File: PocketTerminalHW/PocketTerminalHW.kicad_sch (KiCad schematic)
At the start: 182 parts, among them J1 USB4105-GF-A, J2 DM3D-SF, J3 Conn_01x05, J4 53261-0271, J5 Conn_01x04, J6 Conn_01x02, J7 68712414522, J8 USB4105-GF-A, J9 66011102111302, Q1 BC847BDW1, SW1 K3-1391D-5MM, U1 ESP32-S3-WROOM-1, U2 CP2102N-A02-GQFN28, U3 AMS1117-3.3 / SGM2212-3.3, U4 TP4057, U5 MT3608/SX1308, U6 CC1101RGPR, Y1 3225-26M-SR

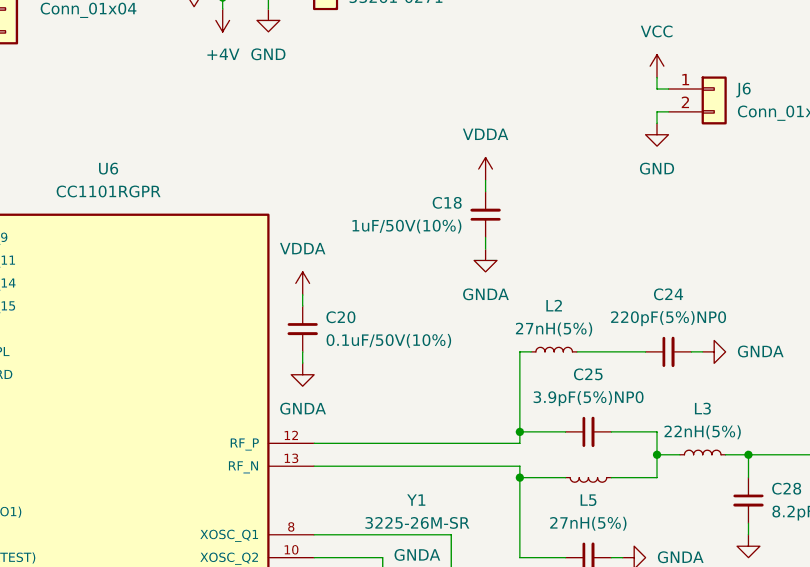
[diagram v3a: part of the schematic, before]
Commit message: Minor cnages to cap values
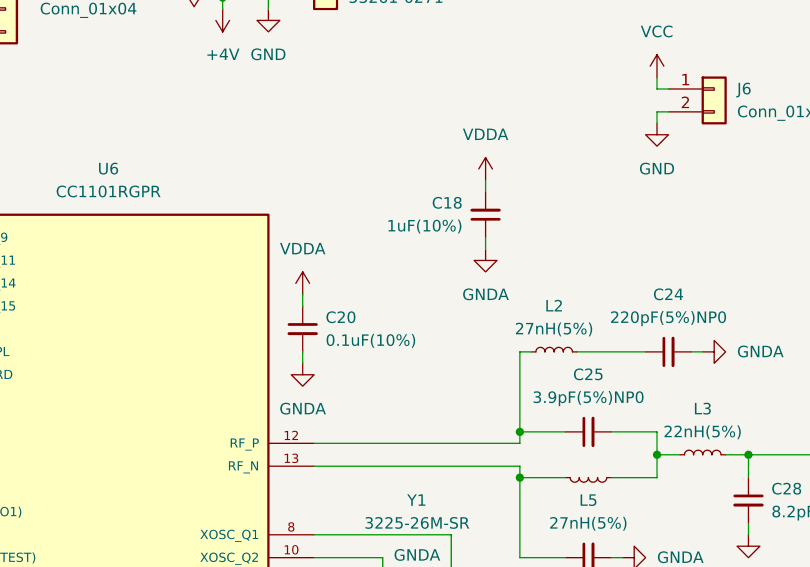
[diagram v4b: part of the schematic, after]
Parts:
- C18: value 1uF/50V(10%) -> 1uF(10%)
- C20: value 0.1uF/50V(10%) -> 0.1uF(10%)
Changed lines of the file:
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@@
 		(row_heights 2.54 2.54 2.54 2.54 2.54)
 		(cells
-			(table_cell "EN"
+			(table_cell "IO0"
 				(exclude_from_sim no)
-				(at 170.18 127 0)
+				(at 175.26 127 0)
 				(size 5.08 2.54)
 				(margins 0.9525 0.9525 0.9525 0.9525)
@@
 			(table_cell "1"
 				(exclude_from_sim no)
-				(at 170.18 129.54 0)
+				(at 175.26 129.54 0)
 				(size 5.08 2.54)
 				(margins 0.9525 0.9525 0.9525 0.9525)
@@
 			(table_cell "1"
 				(exclude_from_sim no)
-				(at 170.18 132.08 0)
+				(at 175.26 132.08 0)
 				(size 5.08 2.54)
 				(margins 0.9525 0.9525 0.9525 0.9525)
@@
 				)
 			)
-			(table_cell "0"
+			(table_cell "1"
 				(exclude_from_sim no)
-				(at 170.18 134.62 0)
+				(at 175.26 134.62 0)
 				(size 5.08 2.54)
 				(margins 0.9525 0.9525 0.9525 0.9525)
@@
 				)
 			)
-			(table_cell "1"
+			(table_cell "0"
 				(exclude_from_sim no)
-				(at 170.18 137.16 0)
+				(at 175.26 137.16 0)
 				(size 5.08 2.54)
 				(margins 0.9525 0.9525 0.9525 0.9525)
@@
 		(row_heights 2.54 2.54 2.54 2.54 2.54)
 		(cells
-			(table_cell "IO0"
+			(table_cell "DTR"
 				(exclude_from_sim no)
-				(at 175.26 127 0)
+				(at 160.02 127 0)
 				(size 5.08 2.54)
 				(margins 0.9525 0.9525 0.9525 0.9525)
@@
 			(table_cell "1"
 				(exclude_from_sim no)
-				(at 175.26 129.54 0)
+				(at 160.02 129.54 0)
 				(size 5.08 2.54)
 				(margins 0.9525 0.9525 0.9525 0.9525)
@@
 				)
 			)
-			(table_cell "1"
+			(table_cell "0"
 				(exclude_from_sim no)
-				(at 175.26 132.08 0)
+				(at 160.02 132.08 0)
 				(size 5.08 2.54)
 				(margins 0.9525 0.9525 0.9525 0.9525)
@@
 			(table_cell "1"
 				(exclude_from_sim no)
-				(at 175.26 134.62 0)
+				(at 160.02 134.62 0)
 				(size 5.08 2.54)
 				(margins 0.9525 0.9525 0.9525 0.9525)
@@
 			(table_cell "0"
 				(exclude_from_sim no)
-				(at 175.26 137.16 0)
+				(at 160.02 137.16 0)
 				(size 5.08 2.54)
 				(margins 0.9525 0.9525 0.9525 0.9525)
@@
 		(row_heights 2.54 2.54 2.54 2.54 2.54)
 		(cells
-			(table_cell "DTR"
+			(table_cell "EN"
 				(exclude_from_sim no)
-				(at 160.02 127 0)
+				(at 170.18 127 0)
 				(size 5.08 2.54)
 				(margins 0.9525 0.9525 0.9525 0.9525)
@@
 			(table_cell "1"
 				(exclude_from_sim no)
-				(at 160.02 129.54 0)
+				(at 170.18 129.54 0)
 				(size 5.08 2.54)
 				(margins 0.9525 0.9525 0.9525 0.9525)
@@
 				)
 			)
-			(table_cell "0"
+			(table_cell "1"
 				(exclude_from_sim no)
-				(at 160.02 132.08 0)
+				(at 170.18 132.08 0)
 				(size 5.08 2.54)
 				(margins 0.9525 0.9525 0.9525 0.9525)
@@
 				)
 			)
-			(table_cell "1"
+			(table_cell "0"
 				(exclude_from_sim no)
-				(at 160.02 134.62 0)
+				(at 170.18 134.62 0)
 				(size 5.08 2.54)
 				(margins 0.9525 0.9525 0.9525 0.9525)
@@
 				)
 			)
-			(table_cell "0"
+			(table_cell "1"
 				(exclude_from_sim no)
-				(at 160.02 137.16 0)
+				(at 170.18 137.16 0)
 				(size 5.08 2.54)
 				(margins 0.9525 0.9525 0.9525 0.9525)
@@
 			)
 		)
-		(property "Value" "1uF/50V(10%)"
+		(property "Value" "1uF(10%)"
 			(at 273.05 199.3835 0)
 			(effects
@@
 			)
 		)
-		(property "Value" "0.1uF/50V(10%)"
+		(property "Value" "0.1uF(10%)"
 			(at 257.81 212.0962 0)
 			(effects

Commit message: Second proto WIP
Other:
- note added: "TODO: Add some power circuit to not use battery while charging"
- note added: "TODO: Maybe move components to the front side, under display"
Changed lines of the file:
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@@
 		)
 	)
+	(text "TODO: Maybe move components to the front side, under display"
+		(exclude_from_sim no)
+		(at 311.912 171.958 0)
+		(effects
+			(font
+				(size 1.27 1.27)
+			)
+		)
+	)
+	(text "TODO: Add some power circuit to not use battery while charging"
+		(exclude_from_sim no)
+		(at 312.42 174.244 0)
+		(effects
+			(font
+				(size 1.27 1.27)
+			)
+		)
+	)
 	(text "TODO: Add USB protection"
 		(exclude_from_sim no)
@@
 		(row_heights 2.54 2.54 2.54 2.54 2.54)
 		(cells
-			(table_cell "IO0"
+			(table_cell "RTS"
 				(exclude_from_sim no)
-				(at 175.26 127 0)
+				(at 165.1 127 0)
 				(size 5.08 2.54)
 				(margins 0.9525 0.9525 0.9525 0.9525)
@@
 			(table_cell "1"
 				(exclude_from_sim no)
-				(at 175.26 129.54 0)
+				(at 165.1 129.54 0)
 				(size 5.08 2.54)
 				(margins 0.9525 0.9525 0.9525 0.9525)
@@
 				)
 			)
-			(table_cell "1"
+			(table_cell "0"
 				(exclude_from_sim no)
-				(at 175.26 132.08 0)
+				(at 165.1 132.08 0)
 				(size 5.08 2.54)
 				(margins 0.9525 0.9525 0.9525 0.9525)
@@
 				)
 			)
-			(table_cell "1"
+			(table_cell "0"
 				(exclude_from_sim no)
-				(at 175.26 134.62 0)
+				(at 165.1 134.62 0)
 				(size 5.08 2.54)
 				(margins 0.9525 0.9525 0.9525 0.9525)
@@
 				)
 			)
-			(table_cell "0"
+			(table_cell "1"
 				(exclude_from_sim no)
-				(at 175.26 137.16 0)
+				(at 165.1 137.16 0)
 				(size 5.08 2.54)
 				(margins 0.9525 0.9525 0.9525 0.9525)
@@
 	)
 	(table
-		(column_count 1)
+		(column_count 2)
 		(border
 			(external yes)
@@
 			)
 		)
-		(column_widths 5.08)
-		(row_heights 2.54 2.54 2.54 2.54 2.54)
+		(column_widths 5.715 6.985)
+		(row_heights 2.54 2.54 2.54 2.54 2.54 2.54)
 		(cells
-			(table_cell "DTR"
+			(table_cell "R"
 				(exclude_from_sim no)
-				(at 160.02 127 0)
-				(size 5.08 2.54)
+				(at 317.5 152.4 0)
+				(size 5.715 2.54)
 				(margins 0.9525 0.9525 0.9525 0.9525)
 				(span 1 1)
@@
 						(size 1.27 1.27)
 					)
-					(justify left top)
+					(justify top)
 				)
 			)
-			(table_cell "1"
+			(table_cell "I"
 				(exclude_from_sim no)
-				(at 160.02 129.54 0)
-				(size 5.08 2.54)
+				(at 323.215 152.4 0)
+				(size 6.985 2.54)
 				(margins 0.9525 0.9525 0.9525 0.9525)
 				(span 1 1)
@@
 						(size 1.27 1.27)
 					)
-					(justify left top)
+					(justify top)
 				)
 			)
-			(table_cell "0"
+			(table_cell "5K"
 				(exclude_from_sim no)
-				(at 160.02 132.08 0)
-				(size 5.08 2.54)
+				(at 317.5 154.94 0)
+				(size 5.715 2.54)
 				(margins 0.9525 0.9525 0.9525 0.9525)
 				(span 1 1)
@@
 				)
 			)
-			(table_cell "1"
+			(table_cell "0.2A"
 				(exclude_from_sim no)
-				(at 160.02 134.62 0)
-				(size 5.08 2.54)
+				(at 323.215 154.94 0)
+				(size 6.985 2.54)
 				(margins 0.9525 0.9525 0.9525 0.9525)
 				(span 1 1)
@@
 				)
 			)
-			(table_cell "0"
+			(table_cell "4K"
 				(exclude_from_sim no)
-				(at 160.02 137.16 0)
-				(size 5.08 2.54)
+				(at 317.5 157.48 0)
+				(size 5.715 2.54)
 				(margins 0.9525 0.9525 0.9525 0.9525)
 				(span 1 1)
@@
 				)
 			)
-		)
-	)
-	(table
-		(column_count 2)
-		(border
-			(external yes)
-			(header yes)
-			(stroke
-				(width 0)
-				(type solid)
-			)
-		)
-		(separators
-			(rows yes)
-			(cols yes)
-			(stroke
-				(width 0)
-				(type solid)
-			)
-		)
-		(column_widths 5.715 6.985)
-		(row_heights 2.54 2.54 2.54 2.54 2.54 2.54)
-		(cells
-			(table_cell "R"
+			(table_cell "0.25A"
 				(exclude_from_sim no)
-				(at 317.5 152.4 0)
-				(size 5.715 2.54)
+				(at 323.215 157.48 0)
+				(size 6.985 2.54)
 				(margins 0.9525 0.9525 0.9525 0.9525)
 				(span 1 1)
@@
 						(size 1.27 1.27)
 					)
-					(justify top)
+					(justify left top)
 				)
 			)
-			(table_cell "I"
+			(table_cell "3K"
 				(exclude_from_sim no)
-				(at 323.215 152.4 0)
-				(size 6.985 2.54)
+				(at 317.5 160.02 0)
+				(size 5.715 2.54)
 				(margins 0.9525 0.9525 0.9525 0.9525)
 				(span 1 1)
@@
 						(size 1.27 1.27)
 					)
-					(justify top)
+					(justify left top)
 				)
 			)
-			(table_cell "5K"
+			(table_cell "0.3A"
 				(exclude_from_sim no)
-				(at 317.5 154.94 0)
-				(size 5.715 2.54)
+				(at 323.215 160.02 0)
+				(size 6.985 2.54)
 				(margins 0.9525 0.9525 0.9525 0.9525)
 				(span 1 1)
@@
 				)
 			)
-			(table_cell "0.2A"
+			(table_cell "2K"
 				(exclude_from_sim no)
-				(at 323.215 154.94 0)
-				(size 6.985 2.54)
+				(at 317.5 162.56 0)
+				(size 5.715 2.54)
 				(margins 0.9525 0.9525 0.9525 0.9525)
 				(span 1 1)
@@
 				)
 			)
-			(table_cell "4K"
+			(table_cell "0.4A"
 				(exclude_from_sim no)
-				(at 317.5 157.48 0)
-				(size 5.715 2.54)
+				(at 323.215 162.56 0)
+				(size 6.985 2.54)
 				(margins 0.9525 0.9525 0.9525 0.9525)
 				(span 1 1)
@@
 				)
 			)
-			(table_cell "0.25A"
+			(table_cell "1.6K"
 				(exclude_from_sim no)
-				(at 323.215 157.48 0)
-				(size 6.985 2.54)
+				(at 317.5 165.1 0)
+				(size 5.715 2.54)
 				(margins 0.9525 0.9525 0.9525 0.9525)
 				(span 1 1)
@@
 				)
 			)
-			(table_cell "3K"
+			(table_cell "0.5A"
 				(exclude_from_sim no)
-				(at 317.5 160.02 0)
-				(size 5.715 2.54)
+				(at 323.215 165.1 0)
+				(size 6.985 2.54)
 				(margins 0.9525 0.9525 0.9525 0.9525)
 				(span 1 1)
@@
 				)
 			)
-			(table_cell "0.3A"
+		)
+	)
+	(table
+		(column_count 1)
+		(border
+			(external yes)
+			(header yes)
+			(stroke
+				(width 0)
+				(type solid)
+			)
+		)
+		(separators
+			(rows yes)
+			(cols yes)
+			(stroke
+				(width 0)
+				(type solid)
+			)
+		)
+		(column_widths 5.08)
+		(row_heights 2.54 2.54 2.54 2.54 2.54)
+		(cells
+			(table_cell "IO0"
 				(exclude_from_sim no)
-				(at 323.215 160.02 0)
-				(size 6.985 2.54)
+				(at 175.26 127 0)
+				(size 5.08 2.54)
 				(margins 0.9525 0.9525 0.9525 0.9525)
 				(span 1 1)
@@
 				)
 			)
-			(table_cell "2K"
+			(table_cell "1"
 				(exclude_from_sim no)
-				(at 317.5 162.56 0)
-				(size 5.715 2.54)
+				(at 175.26 129.54 0)
+				(size 5.08 2.54)
 				(margins 0.9525 0.9525 0.9525 0.9525)
 				(span 1 1)
@@
 				)
 			)
-			(table_cell "0.4A"
+			(table_cell "1"
 				(exclude_from_sim no)
-				(at 323.215 162.56 0)
-				(size 6.985 2.54)
+				(at 175.26 132.08 0)
+				(size 5.08 2.54)
 				(margins 0.9525 0.9525 0.9525 0.9525)
 				(span 1 1)
@@
 				)
 			)
-			(table_cell "1.6K"
+			(table_cell "1"
 				(exclude_from_sim no)
-				(at 317.5 165.1 0)
-				(size 5.715 2.54)
+				(at 175.26 134.62 0)
+				(size 5.08 2.54)
 				(margins 0.9525 0.9525 0.9525 0.9525)
 				(span 1 1)
@@
 				)
 			)
-			(table_cell "0.5A"
+			(table_cell "0"
 				(exclude_from_sim no)
-				(at 323.215 165.1 0)
-				(size 6.985 2.54)
+				(at 175.26 137.16 0)
+				(size 5.08 2.54)
 				(margins 0.9525 0.9525 0.9525 0.9525)
 				(span 1 1)
@@
 		(row_heights 2.54 2.54 2.54 2.54 2.54)
 		(cells
-			(table_cell "RTS"
+			(table_cell "EN"
 				(exclude_from_sim no)
-				(at 165.1 127 0)
+				(at 170.18 127 0)
 				(size 5.08 2.54)
 				(margins 0.9525 0.9525 0.9525 0.9525)
@@
 			(table_cell "1"
 				(exclude_from_sim no)
-				(at 165.1 129.54 0)
+				(at 170.18 129.54 0)
 				(size 5.08 2.54)
 				(margins 0.9525 0.9525 0.9525 0.9525)
@@
 				)
 			)
-			(table_cell "0"
+			(table_cell "1"
 				(exclude_from_sim no)
-				(at 165.1 132.08 0)
+				(at 170.18 132.08 0)
 				(size 5.08 2.54)
 				(margins 0.9525 0.9525 0.9525 0.9525)
@@
 			(table_cell "0"
 				(exclude_from_sim no)
-				(at 165.1 134.62 0)
+				(at 170.18 134.62 0)
 				(size 5.08 2.54)
 				(margins 0.9525 0.9525 0.9525 0.9525)
@@
 			(table_cell "1"
 				(exclude_from_sim no)
-				(at 165.1 137.16 0)
+				(at 170.18 137.16 0)
 				(size 5.08 2.54)
 				(margins 0.9525 0.9525 0.9525 0.9525)
@@
 		(row_heights 2.54 2.54 2.54 2.54 2.54)
 		(cells
-			(table_cell "EN"
+			(table_cell "DTR"
 				(exclude_from_sim no)
-				(at 170.18 127 0)
+				(at 160.02 127 0)
 				(size 5.08 2.54)
 				(margins 0.9525 0.9525 0.9525 0.9525)
@@
 			(table_cell "1"
 				(exclude_from_sim no)
-				(at 170.18 129.54 0)
+				(at 160.02 129.54 0)
 				(size 5.08 2.54)
 				(margins 0.9525 0.9525 0.9525 0.9525)
@@
 				)
 			)
-			(table_cell "1"
+			(table_cell "0"
 				(exclude_from_sim no)
-				(at 170.18 132.08 0)
+				(at 160.02 132.08 0)
 				(size 5.08 2.54)
 				(margins 0.9525 0.9525 0.9525 0.9525)
@@
 				)
 			)
-			(table_cell "0"
+			(table_cell "1"
 				(exclude_from_sim no)
-				(at 170.18 134.62 0)
+				(at 160.02 134.62 0)
 				(size 5.08 2.54)
 				(margins 0.9525 0.9525 0.9525 0.9525)
@@
 				)
 			)
-			(table_cell "1"
+			(table_cell "0"
 				(exclude_from_sim no)
-				(at 170.18 137.16 0)
+				(at 160.02 137.16 0)
 				(size 5.08 2.54)
 				(margins 0.9525 0.9525 0.9525 0.9525)
